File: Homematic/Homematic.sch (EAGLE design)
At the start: 27 parts, among them IC1 3.3V, IC2 3.3V, P1 DF11-06-2DS, Q1 BS170

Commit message: Replace trough hole capacitors with smd
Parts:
- C1, C6: device capacitor-wima:C2,5-3 -> rcl:C-EUC0805
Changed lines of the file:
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@@
 <grid distance="0.1" unitdist="inch" unit="inch" style="lines" multiple="1" display="no" altdistance="0.01" altunitdist="inch" altunit="inch"/>
 <layers>
-<layer number="1" name="Top" color="4" fill="1" visible="no" active="no"/>
-<layer number="16" name="Bottom" color="1" fill="1" visible="no" active="no"/>
-<layer number="17" name="Pads" color="2" fill="1" visible="no" active="no"/>
-<layer number="18" name="Vias" color="2" fill="1" visible="no" active="no"/>
-<layer number="19" name="Unrouted" color="6" fill="1" visible="no" active="no"/>
-<layer number="20" name="Dimension" color="15" fill="1" visible="no" active="no"/>
-<layer number="21" name="tPlace" color="7" fill="1" visible="no" active="no"/>
-<layer number="22" name="bPlace" color="7" fill="1" visible="no" active="no"/>
-<layer number="23" name="tOrigins" color="15" fill="1" visible="no" active="no"/>
-<layer number="24" name="bOrigins" color="15" fill="1" visible="no" active="no"/>
-<layer number="25" name="tNames" color="7" fill="1" visible="no" active="no"/>
-<layer number="26" name="bNames" color="7" fill="1" visible="no" active="no"/>
-<layer number="27" name="tValues" color="7" fill="1" visible="no" active="no"/>
-<layer number="28" name="bValues" color="7" fill="1" visible="no" active="no"/>
+<layer number="1" name="Top" color="4" fill="1" visible="yes" active="no"/>
+<layer number="16" name="Bottom" color="1" fill="1" visible="yes" active="no"/>
+<layer number="17" name="Pads" color="2" fill="1" visible="yes" active="no"/>
+<layer number="18" name="Vias" color="2" fill="1" visible="yes" active="no"/>
+<layer number="19" name="Unrouted" color="6" fill="1" visible="yes" active="no"/>
+<layer number="20" name="Dimension" color="15" fill="1" visible="yes" active="no"/>
+<layer number="21" name="tPlace" color="7" fill="1" visible="yes" active="no"/>
+<layer number="22" name="bPlace" color="7" fill="1" visible="yes" active="no"/>
+<layer number="23" name="tOrigins" color="15" fill="1" visible="yes" active="no"/>
+<layer number="24" name="bOrigins" color="15" fill="1" visible="yes" active="no"/>
+<layer number="25" name="tNames" color="7" fill="1" visible="yes" active="no"/>
+<layer number="26" name="bNames" color="7" fill="1" visible="yes" active="no"/>
+<layer number="27" name="tValues" color="7" fill="1" visible="yes" active="no"/>
+<layer number="28" name="bValues" color="7" fill="1" visible="yes" active="no"/>
 <layer number="29" name="tStop" color="7" fill="3" visible="no" active="no"/>
 <layer number="30" name="bStop" color="7" fill="6" visible="no" active="no"/>
@@
 <layer number="35" name="tGlue" color="7" fill="4" visible="no" active="no"/>
 <layer number="36" name="bGlue" color="7" fill="5" visible="no" active="no"/>
-<layer number="37" name="tTest" color="7" fill="1" visible="no" active="no"/>
-<layer number="38" name="bTest" color="7" fill="1" visible="no" active="no"/>
+<layer number="37" name="tTest" color="7" fill="1" visible="yes" active="no"/>
+<layer number="38" name="bTest" color="7" fill="1" visible="yes" active="no"/>
 <layer number="39" name="tKeepout" color="4" fill="11" visible="no" active="no"/>
 <layer number="40" name="bKeepout" color="1" fill="11" visible="no" active="no"/>
@@
 <layer number="44" name="Drills" color="7" fill="1" visible="no" active="no"/>
 <layer number="45" name="Holes" color="7" fill="1" visible="no" active="no"/>
-<layer number="46" name="Milling" color="3" fill="1" visible="no" active="no"/>
-<layer number="47" name="Measures" color="7" fill="1" visible="no" active="no"/>
-<layer number="48" name="Document" color="7" fill="1" visible="no" active="no"/>
-<layer number="49" name="Reference" color="7" fill="1" visible="no" active="no"/>
-<layer number="50" name="dxf" color="7" fill="1" visible="no" active="no"/>
-<layer number="51" name="tDocu" color="7" fill="1" visible="no" active="no"/>
-<layer number="52" name="bDocu" color="7" fill="1" visible="no" active="no"/>
-<layer number="53" name="tGND_GNDA" color="7" fill="9" visible="no" active="no"/>
-<layer number="54" name="bGND_GNDA" color="1" fill="9" visible="no" active="no"/>
-<layer number="56" name="wert" color="7" fill="1" visible="no" active="no"/>
-<layer number="57" name="tCAD" color="7" fill="1" visible="no" active="no"/>
-<layer number="59" name="tCarbon" color="7" fill="1" visible="no" active="no"/>
-<layer number="60" name="bCarbon" color="7" fill="1" visible="no" active="no"/>
+<layer number="46" name="Milling" color="3" fill="1" visible="yes" active="no"/>
+<layer number="47" name="Measures" color="7" fill="1" visible="yes" active="no"/>
+<layer number="48" name="Document" color="7" fill="1" visible="yes" active="no"/>
+<layer number="49" name="Reference" color="7" fill="1" visible="yes" active="no"/>
+<layer number="50" name="dxf" color="7" fill="1" visible="yes" active="no"/>
+<layer number="51" name="tDocu" color="7" fill="1" visible="yes" active="no"/>
+<layer number="52" name="bDocu" color="7" fill="1" visible="yes" active="no"/>
+<layer number="53" name="tGND_GNDA" color="7" fill="9" visible="yes" active="no"/>
+<layer number="54" name="bGND_GNDA" color="1" fill="9" visible="yes" active="no"/>
+<layer number="56" name="wert" color="7" fill="1" visible="yes" active="no"/>
+<layer number="57" name="tCAD" color="7" fill="1" visible="yes" active="no"/>
+<layer number="59" name="tCarbon" color="7" fill="1" visible="yes" active="no"/>
+<layer number="60" name="bCarbon" color="7" fill="1" visible="yes" active="no"/>
 <layer number="90" name="Modules" color="5" fill="1" visible="yes" active="yes"/>
 <layer number="91" name="Nets" color="2" fill="1" visible="yes" active="yes"/>
@@
 <part name="P+2" library="supply1" deviceset="+5V" device=""/>
 <part name="P+3" library="supply1" deviceset="+5V" device=""/>
-<part name="C6" library="capacitor-wima" deviceset="C" device="2,5-3" value="100nF"/>
+<part name="C6" library="rcl" deviceset="C-EU" device="C0805" value="100nF"/>
 <part name="R2" library="rcl" deviceset="R-EU_" device="0204/7" value="10K">
 <attribute name="MF" value=""/>
@@
 </part>
 <part name="GND6" library="supply1" deviceset="GND" device=""/>
-<part name="C1" library="capacitor-wima" deviceset="C" device="2,5-3" value="100nF"/>
+<part name="C1" library="rcl" deviceset="C-EU" device="C0805" value="100nF"/>
 <part name="P+4" library="supply1" deviceset="+5V" device=""/>
 <part name="+3V1" library="supply1" deviceset="+3V3" device=""/>

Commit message: Generate gerber files.
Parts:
- added F3: 3A, SparkFun-PowerIC:PTCPTH
- D3: value SB2H100 -> MURS320; device diode:DIODE-DO41-7.6 -> diode:DIODE-SMC
- F1, F2: value PTCPTH -> 2A
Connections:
- new net N$9: D3.C, F3.2
- net N$7: now also F3.1; no longer D3.C
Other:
- moved on the sheet: MP1584-1, MP1584-2
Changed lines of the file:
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@@
 <part name="D1" library="diode" deviceset="1N5908" device=""/>
 <part name="D2" library="diode" deviceset="1N5908" device=""/>
-<part name="F1" library="SparkFun-PowerIC" deviceset="PTC" device="PTH"/>
-<part name="F2" library="SparkFun-PowerIC" deviceset="PTC" device="PTH"/>
+<part name="F1" library="SparkFun-PowerIC" deviceset="PTC" device="PTH" value="2A"/>
+<part name="F2" library="SparkFun-PowerIC" deviceset="PTC" device="PTH" value="2A"/>
 <part name="GND1" library="supply1" deviceset="GND" device=""/>
 <part name="P+1" library="supply1" deviceset="+24V" device=""/>
@@
 <part name="MP1584-2" library="modules" deviceset="DC-DC-STEP-DOWN-MP1584" device=""/>
 <part name="MP1584-1" library="modules" deviceset="DC-DC-STEP-DOWN-MP1584" device=""/>
-<part name="D3" library="diode" deviceset="DIODE-" device="DO41-7.6" value="SB2H100"/>
+<part name="D3" library="diode" deviceset="DIODE-" device="SMC" value="MURS320"/>
 <part name="RXB8" library="modules" deviceset="WIRELESS-RXB8-5V" device=""/>
 <part name="GND3" library="supply1" deviceset="GND" device=""/>
@@
 <part name="C7" library="capacitor-wima" deviceset="C" device="2,5-3" value="100nF"/>
 <part name="GND7" library="supply1" deviceset="GND" device=""/>
+<part name="F3" library="SparkFun-PowerIC" deviceset="PTC" device="PTH" value="3A"/>
 </parts>
 <sheets>
@@
 <instance part="F1" gate="G$1" x="83.82" y="99.06" rot="R180"/>
 <instance part="F2" gate="G$1" x="81.28" y="58.42"/>
-<instance part="GND1" gate="1" x="63.5" y="78.74" rot="R270"/>
+<instance part="GND1" gate="1" x="68.58" y="78.74" rot="R270"/>
 <instance part="P+1" gate="1" x="20.32" y="73.66" smashed="yes" rot="R180">
 <attribute name="VALUE" x="20.32" y="71.12" size="1.778" layer="96" rot="R180" align="center"/>
@@
 <attribute name="MPN" x="193.04" y="17.78" size="1.778" layer="96" rot="MR270" display="off"/>
 </instance>
-<instance part="MP1584-2" gate="G$1" x="50.8" y="93.98"/>
-<instance part="MP1584-1" gate="G$1" x="50.8" y="63.5" rot="MR180"/>
+<instance part="MP1584-2" gate="G$1" x="58.42" y="93.98" smashed="yes">
+<attribute name="NAME" x="49.42" y="108.77" size="1.778" layer="95"/>
+<attribute name="VALUE" x="49.42" y="106.02" size="1.778" layer="96"/>
+</instance>
+<instance part="MP1584-1" gate="G$1" x="58.42" y="63.5" smashed="yes" rot="MR180">
+<attribute name="NAME" x="49.42" y="48.71" size="1.778" layer="95" rot="MR180"/>
+<attribute name="VALUE" x="49.42" y="51.46" size="1.778" layer="96" rot="MR180"/>
+</instance>
 <instance part="D3" gate="G$1" x="25.4" y="81.28" smashed="yes">
-<attribute name="NAME" x="27.94" y="79.2226" size="1.778" layer="95"/>
+<attribute name="NAME" x="25.4" y="76.6826" size="1.778" layer="95"/>
 <attribute name="VALUE" x="25.4" y="84.0486" size="1.778" layer="96" align="bottom-center"/>
 </instance>
@@
 </instance>
 <instance part="GND7" gate="1" x="177.8" y="58.42"/>
+<instance part="F3" gate="G$1" x="35.56" y="81.28" rot="R180"/>
 </instances>
 <busses>
@@
 <segment>
 <pinref part="GND1" gate="1" pin="GND"/>
-<wire x1="66.04" y1="78.74" x2="68.58" y2="78.74" width="0.1524" layer="91"/>
+<wire x1="71.12" y1="78.74" x2="73.66" y2="78.74" width="0.1524" layer="91"/>
 <pinref part="D2" gate="1" pin="A"/>
-<wire x1="68.58" y1="78.74" x2="88.9" y2="78.74" width="0.1524" layer="91"/>
+<wire x1="73.66" y1="78.74" x2="88.9" y2="78.74" width="0.1524" layer="91"/>
 <wire x1="88.9" y1="78.74" x2="88.9" y2="76.2" width="0.1524" layer="91"/>
 <pinref part="D1" gate="1" pin="A"/>
@@
 <junction x="96.52" y="73.66"/>
 <pinref part="MP1584-2" gate="G$1" pin="OUT-"/>
-<wire x1="66.04" y1="88.9" x2="68.58" y2="88.9" width="0.1524" layer="91"/>
-<wire x1="68.58" y1="88.9" x2="68.58" y2="78.74" width="0.1524" layer="91"/>
+<wire x1="73.66" y1="88.9" x2="73.66" y2="78.74" width="0.1524" layer="91"/>
 <pinref part="MP1584-1" gate="G$1" pin="OUT-"/>
-<wire x1="66.04" y1="68.58" x2="68.58" y2="68.58" width="0.1524" layer="91"/>
-<wire x1="68.58" y1="68.58" x2="68.58" y2="78.74" width="0.1524" layer="91"/>
-<junction x="68.58" y="78.74"/>
+<wire x1="73.66" y1="68.58" x2="73.66" y2="78.74" width="0.1524" layer="91"/>
+<junction x="73.66" y="78.74"/>
 <wire x1="96.52" y1="45.72" x2="101.6" y2="45.72" width="0.1524" layer="91"/>
 <pinref part="IC1" gate="1" pin="GND"/>
@@
 <wire x1="15.24" y1="68.58" x2="15.24" y2="66.04" width="0.1524" layer="91"/>
 <pinref part="MP1584-1" gate="G$1" pin="IN-"/>
-<wire x1="15.24" y1="68.58" x2="35.56" y2="68.58" width="0.1524" layer="91"/>
+<wire x1="15.24" y1="68.58" x2="43.18" y2="68.58" width="0.1524" layer="91"/>
 <junction x="15.24" y="68.58"/>
 <pinref part="GND3" gate="1" pin="GND"/>
@@
 <junction x="15.24" y="78.74"/>
 <pinref part="MP1584-2" gate="G$1" pin="IN-"/>
-<wire x1="15.24" y1="88.9" x2="35.56" y2="88.9" width="0.1524" layer="91"/>
+<wire x1="15.24" y1="88.9" x2="43.18" y2="88.9" width="0.1524" layer="91"/>
 </segment>
 <segment>
@@
 <pinref part="MP1584-2" gate="G$1" pin="OUT+"/>
 <pinref part="F1" gate="G$1" pin="2"/>
-<wire x1="66.04" y1="99.06" x2="76.2" y2="99.06" width="0.1524" layer="91"/>
+<wire x1="73.66" y1="99.06" x2="76.2" y2="99.06" width="0.1524" layer="91"/>
 </segment>
 </net>
@@
 <pinref part="MP1584-1" gate="G$1" pin="OUT+"/>
 <pinref part="F2" gate="G$1" pin="1"/>
-<wire x1="66.04" y1="58.42" x2="76.2" y2="58.42" width="0.1524" layer="91"/>
+<wire x1="73.66" y1="58.42" x2="76.2" y2="58.42" width="0.1524" layer="91"/>
 </segment>
 </net>
@@
 <net name="N$7" class="0">
 <segment>
+<pinref part="MP1584-2" gate="G$1" pin="IN+"/>
+<wire x1="40.64" y1="99.06" x2="43.18" y2="99.06" width="0.1524" layer="91"/>
+<wire x1="40.64" y1="99.06" x2="40.64" y2="81.28" width="0.1524" layer="91"/>
+<pinref part="MP1584-1" gate="G$1" pin="IN+"/>
+<wire x1="40.64" y1="81.28" x2="40.64" y2="58.42" width="0.1524" layer="91"/>
+<wire x1="40.64" y1="58.42" x2="43.18" y2="58.42" width="0.1524" layer="91"/>
+<pinref part="F3" gate="G$1" pin="1"/>
+<junction x="40.64" y="81.28"/>
+</segment>
+</net>
+<net name="N$9" class="0">
+<segment>
 <pinref part="D3" gate="G$1" pin="C"/>
-<wire x1="27.94" y1="81.28" x2="33.02" y2="81.28" width="0.1524" layer="91"/>
-<wire x1="33.02" y1="81.28" x2="33.02" y2="99.06" width="0.1524" layer="91"/>
-<pinref part="MP1584-2" gate="G$1" pin="IN+"/>
-<wire x1="33.02" y1="99.06" x2="35.56" y2="99.06" width="0.1524" layer="91"/>
-<wire x1="33.02" y1="81.28" x2="33.02" y2="58.42" width="0.1524" layer="91"/>
-<pinref part="MP1584-1" gate="G$1" pin="IN+"/>
-<wire x1="33.02" y1="58.42" x2="35.56" y2="58.42" width="0.1524" layer="91"/>
-<junction x="33.02" y="81.28"/>
-</segment>
-</net>
+<pinref part="F3" gate="G$1" pin="2"/>
+</segment>
+</net>

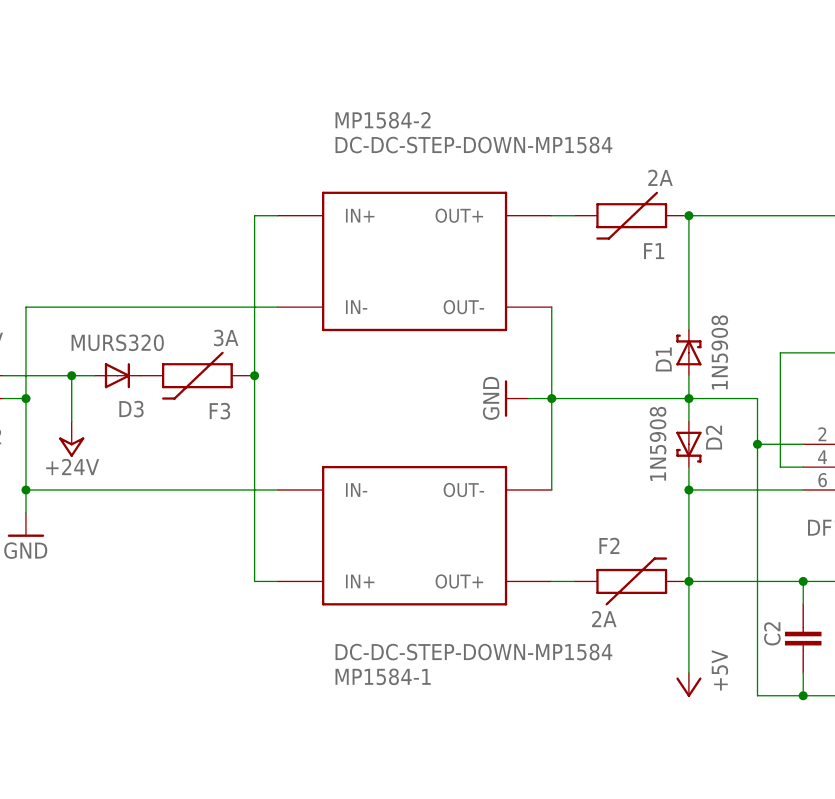
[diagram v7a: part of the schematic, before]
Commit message: Fix PTC size.
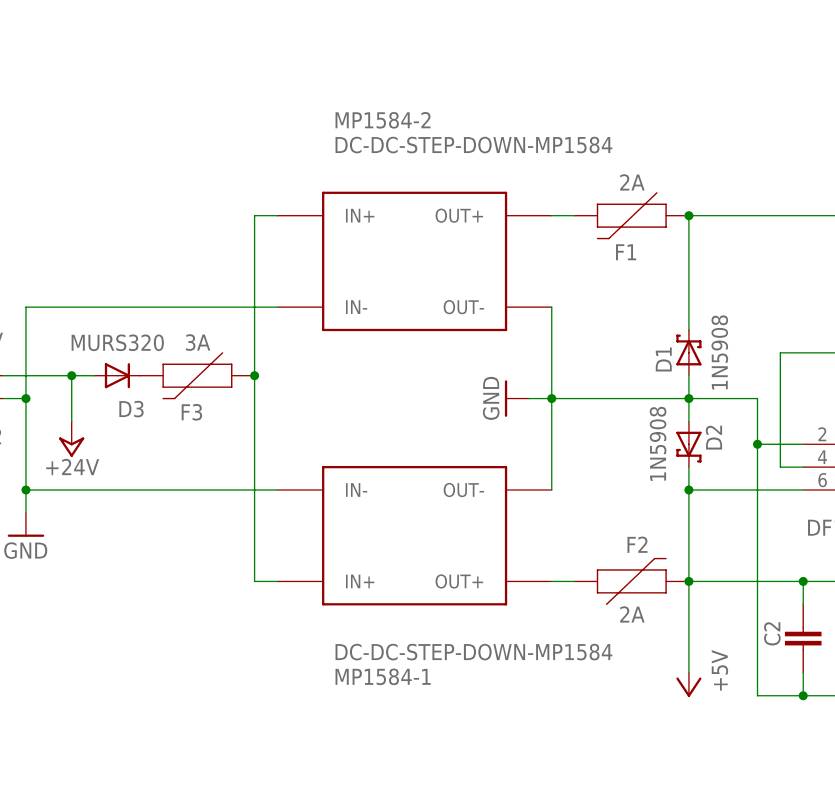
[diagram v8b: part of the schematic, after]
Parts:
- F1, F2: device SparkFun-PowerIC:PTCPTH -> SparkFun-Fuses:PPTCPTH
- F3: device SparkFun-PowerIC:PTCPTH -> SparkFun-Fuses:PPTCPTH11MM
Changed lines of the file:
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@@
 <part name="D1" library="diode" deviceset="1N5908" device=""/>
 <part name="D2" library="diode" deviceset="1N5908" device=""/>
-<part name="F1" library="SparkFun-PowerIC" deviceset="PTC" device="PTH" value="2A"/>
-<part name="F2" library="SparkFun-PowerIC" deviceset="PTC" device="PTH" value="2A"/>
+<part name="F1" library="SparkFun-Fuses" deviceset="PPTC" device="PTH" value="2A"/>
+<part name="F2" library="SparkFun-Fuses" deviceset="PPTC" device="PTH" value="2A"/>
 <part name="GND1" library="supply1" deviceset="GND" device=""/>
 <part name="P+1" library="supply1" deviceset="+24V" device=""/>
@@
 <part name="C7" library="capacitor-wima" deviceset="C" device="2,5-3" value="100nF"/>
 <part name="GND7" library="supply1" deviceset="GND" device=""/>
-<part name="F3" library="SparkFun-PowerIC" deviceset="PTC" device="PTH" value="3A"/>
+<part name="F3" library="SparkFun-Fuses" deviceset="PPTC" device="PTH11MM" value="3A"/>
 </parts>
 <sheets>
